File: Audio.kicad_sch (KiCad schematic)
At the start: 17 parts, among them CN2 PJ-3537S, U3 SGTL5000XNAA3R2, U8 PCM1807PW

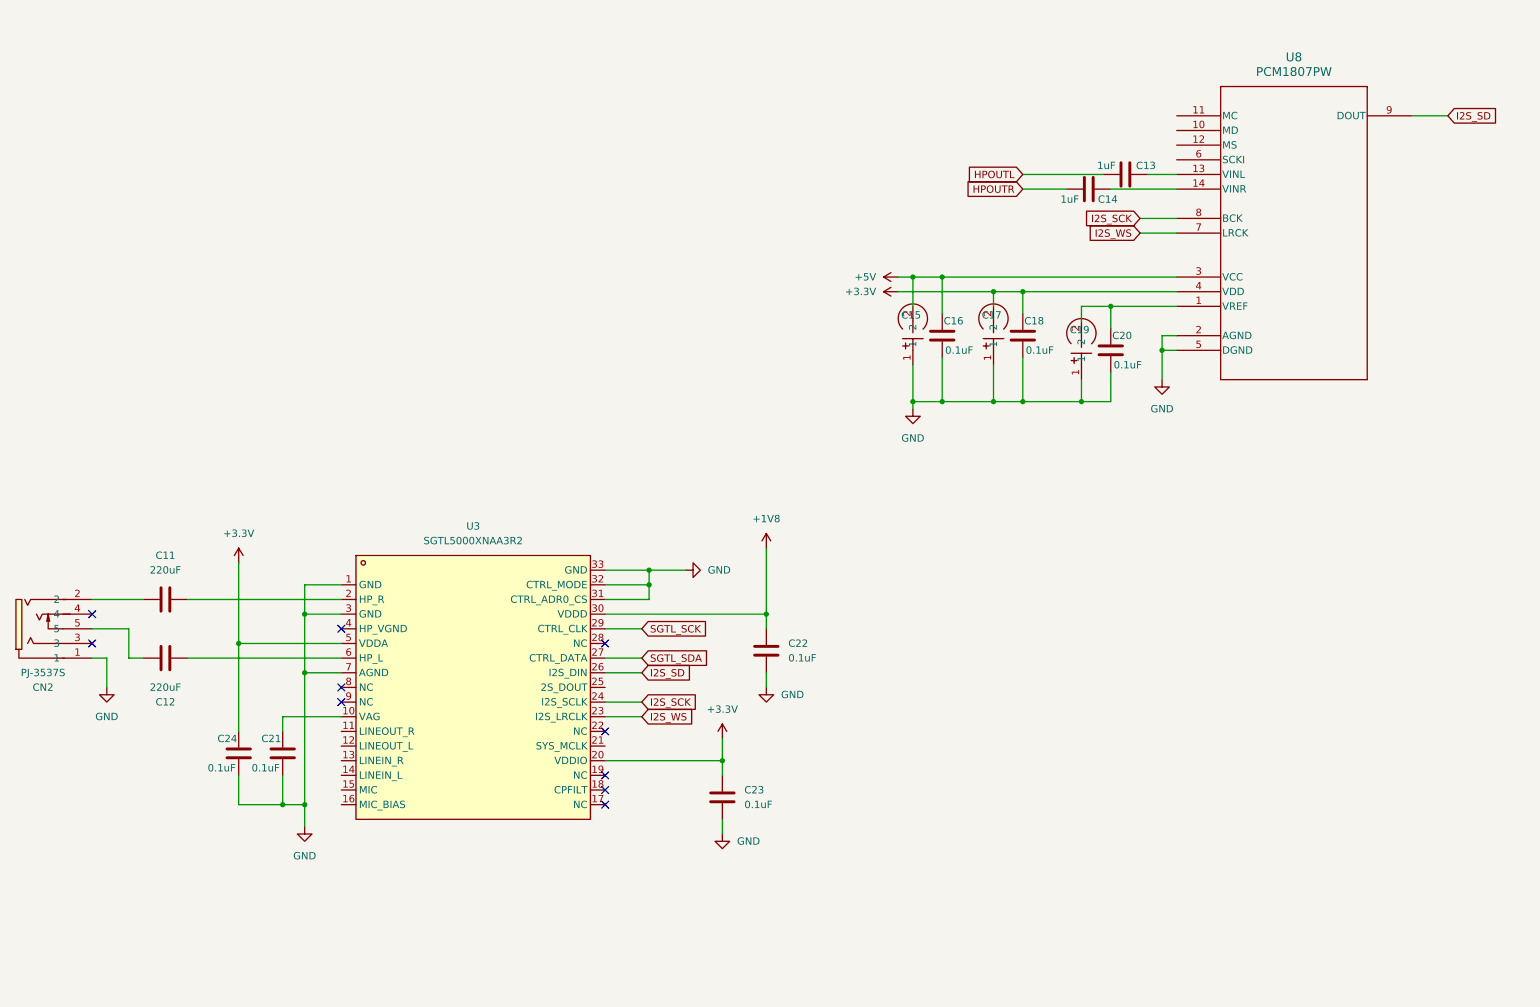
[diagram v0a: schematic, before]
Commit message: power changes, audio changes, testing layout
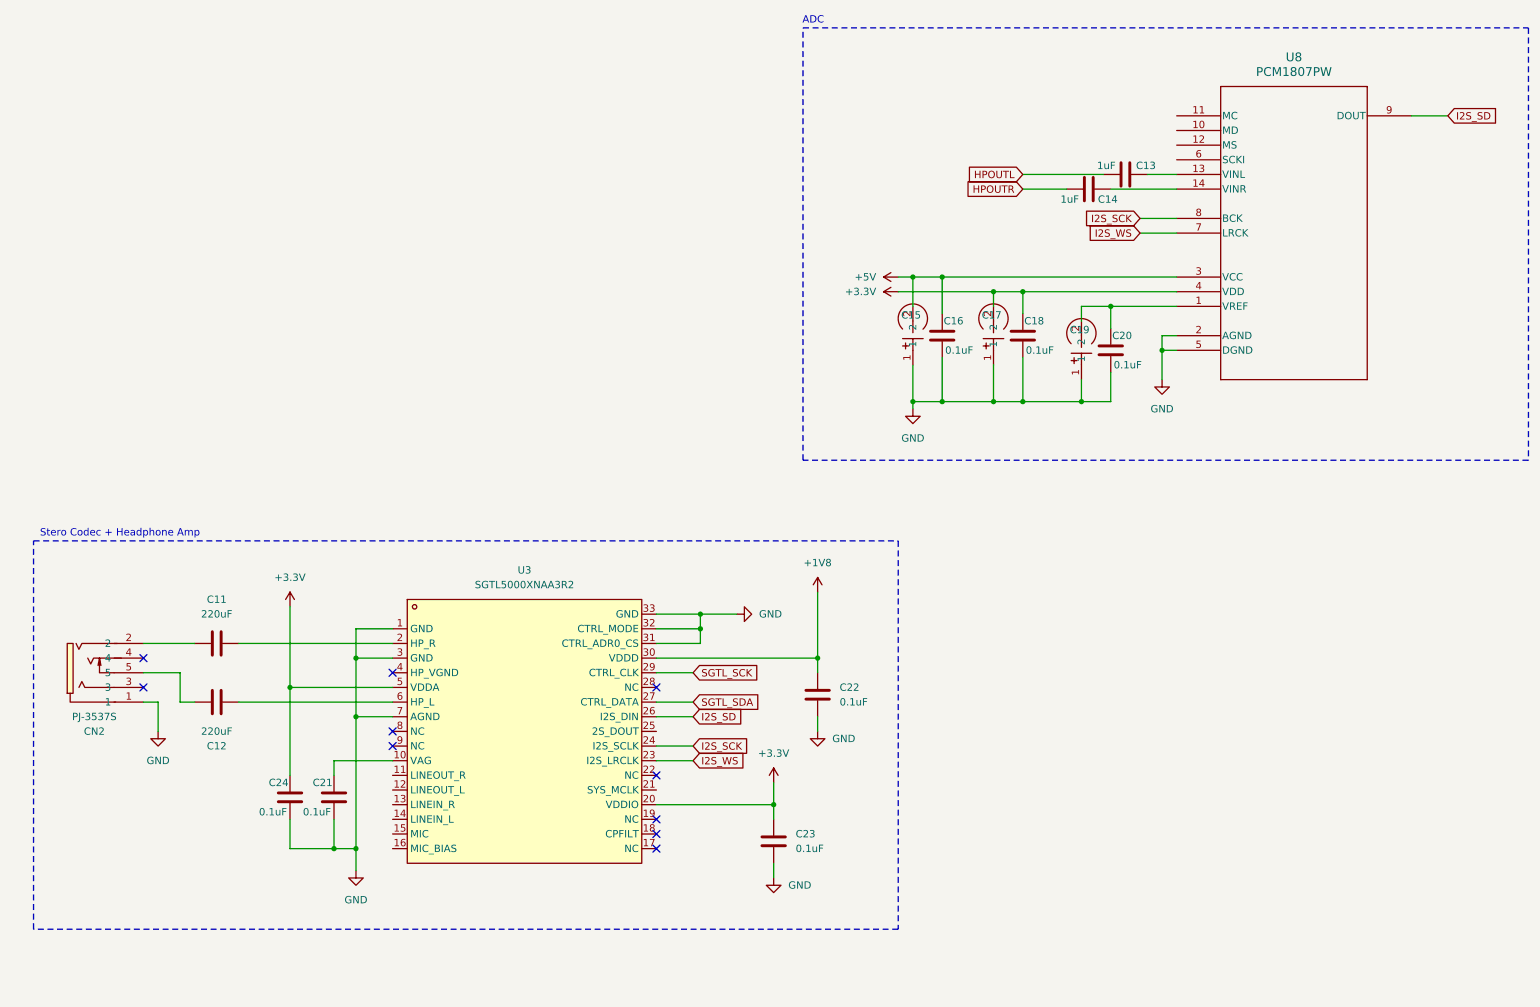
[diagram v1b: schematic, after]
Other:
- note added: "ADC"
- note added: "Stero Codec + Headphone Amp"
- moved on the sheet: C11, C12, C21, C22, C23, C24, CN2, U3

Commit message: audio changes, better layout
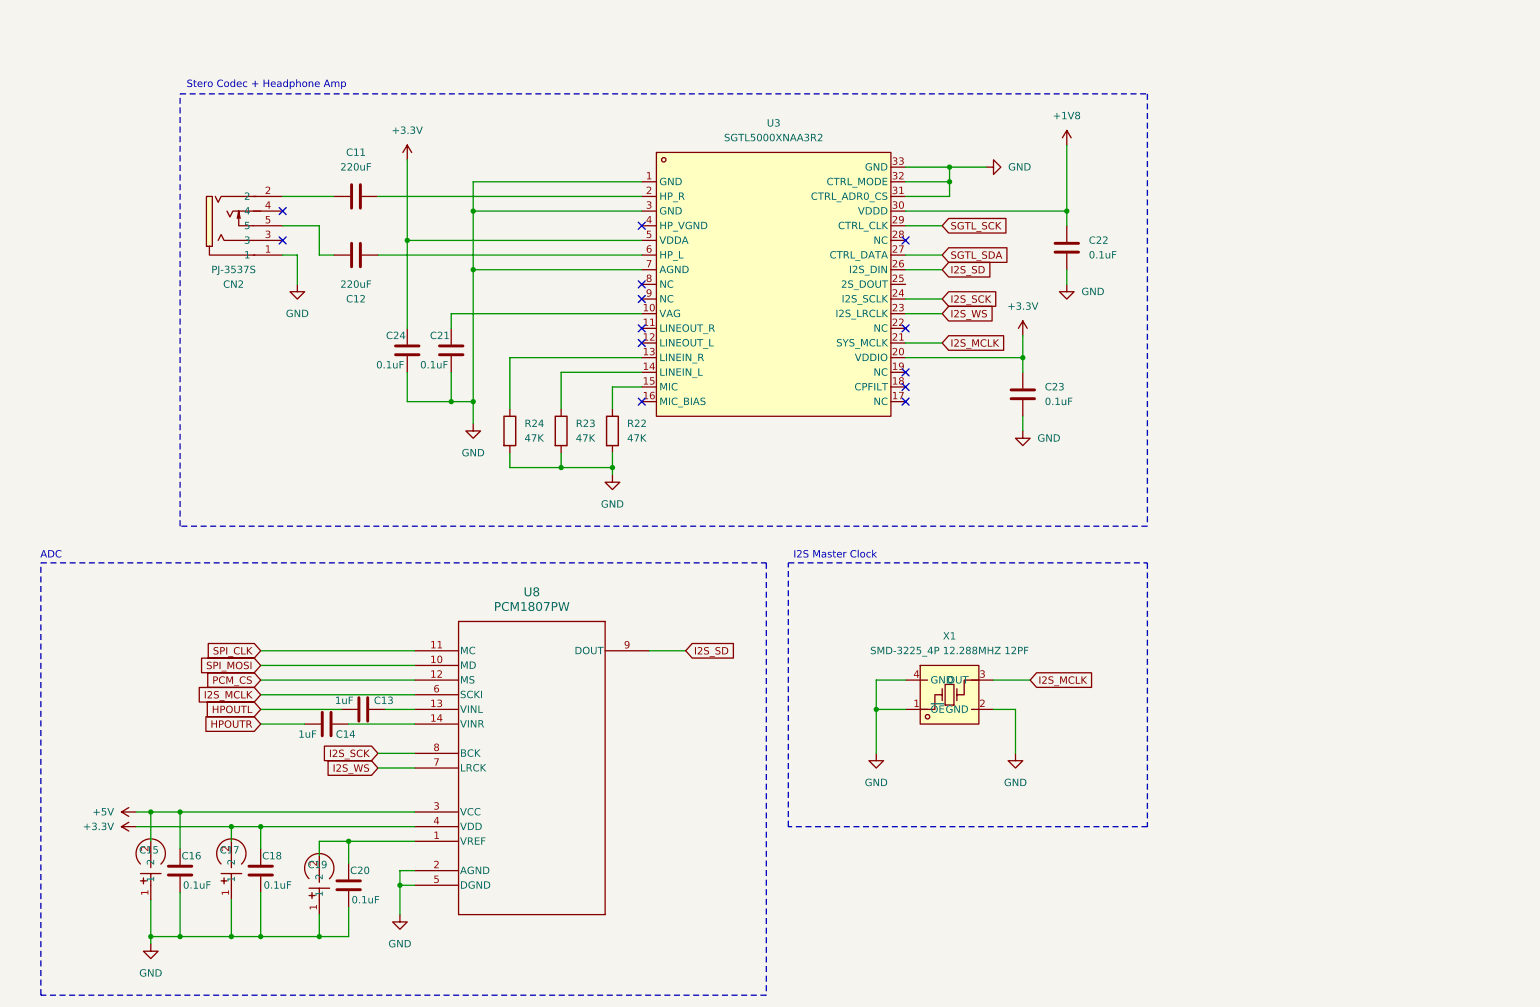
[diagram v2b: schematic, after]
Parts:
- added R22, R23, R24: 47K, symbol Device:R
- added X1: SMD-3225_4P 12.288MHZ 12PF, easyeda2kicad:CRYSTAL-SMD_4P-L3.2-W2.5-BL-2, symbol easyeda2kicad:SMD-3225_4P12.288MHZ12PF
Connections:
- net GND: now also R22.2, R23.2, R24.2, X1.1 (~{OE}), X1.2 (GND), X1.4 (GND)
- net at U3.13 (LINEIN_R): now also R24.1
- net at U3.14 (LINEIN_L): now also R23.1
- net at U3.15 (MIC): now also R22.1
- net I2S_MCLK: now reaches U3.21 (SYS_MCLK)
- net I2S_MCLK: now also U8.6 (SCKI), X1.3 (OUT)
- net SPI_MOSI: now reaches U8.10 (MD)
- net SPI_CLK: now reaches U8.11 (MC)
- net PCM_CS: now reaches U8.12 (MS)
- no-connect marks 10 -> 13
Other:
- note added: "I2S Master Clock"
- moved on the sheet: C11, C12, C13, C14, C15, C16, C17, C18, C19, C20, C21, C22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

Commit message: start of adding esp32 module
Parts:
- removed X1: SMD-3225_4P 12.288MHZ 12PF, easyeda2kicad:CRYSTAL-SMD_4P-L3.2-W2.5-BL-2, symbol easyeda2kicad:SMD-3225_4P12.288MHZ12PF
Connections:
- net I2S_SD renamed I2S_PCMOUT
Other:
- note removed: "I2S Master Clock"

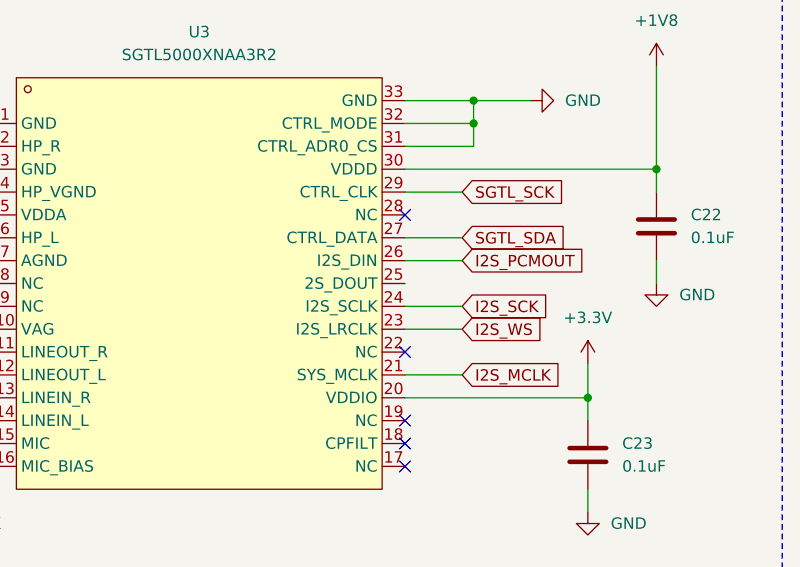
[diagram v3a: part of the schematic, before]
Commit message: power changes to v3s, nand
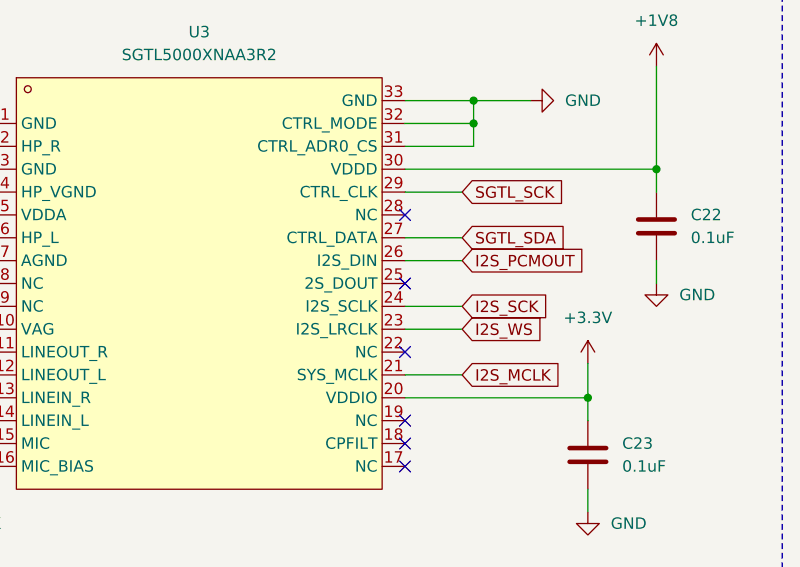
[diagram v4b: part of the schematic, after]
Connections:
- no-connect marks 13 -> 14
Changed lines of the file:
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@@
+	)
+	(no_connect
+		(at 172.72 64.77)
 	)
 	(no_connect

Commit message: power changes for v3s, cleanup
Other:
- title: (none) -> iPodClone
- moved on the sheet: C11, C12, C21, C22, C23, C24, CN2, R22, R23, R24, U3

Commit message: gitignore and audio changes
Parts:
- removed C15, C17, C19: GVS1H100M0604, easyeda2kicad:CAP-SMD_BD6.3-L6.6-W6.6-LS7.3, symbol easyeda2kicad:GVS1H100M0604
- removed CN2: PJ-3537S, easyeda2kicad:AUDIO-SMD_PJ-3537S, symbol easyeda2kicad:PJ-3537S
- added C52, C53, C54: 10uF, symbol Device:C
- added CN3: PJ-342, easyeda2kicad:AUDIO-SMD_PJ-342, symbol easyeda2kicad:PJ-342
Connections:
- net +3.3V: now also C52.1
- net +5V: now also C53.1
- net GND: now also C52.2, C53.2, C54.2
- net at C20.1, U8.1 (VREF): now also C54.1
- net at C12.1: now also CN3.5
- net at C11.1: now also CN3.4
- net SGTL_SCK renamed I2C_SCK
- net SGTL_SDA renamed I2C_SDA
